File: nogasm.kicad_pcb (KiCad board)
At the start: 2 copper layers, 76.2 x 76.2 mm, 59 parts, among them J1 DC Jack PJ-031DH 3.5mm, J2 DC Jack PRT-10811, Q1 BUK92150-55A, Q2 MMBT2222A, Q3 MMBT2222A, Q4 MMBT2222A, U1 WS2812B, U10 WS2812B, U11 WS2812B, U12 WS2812B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

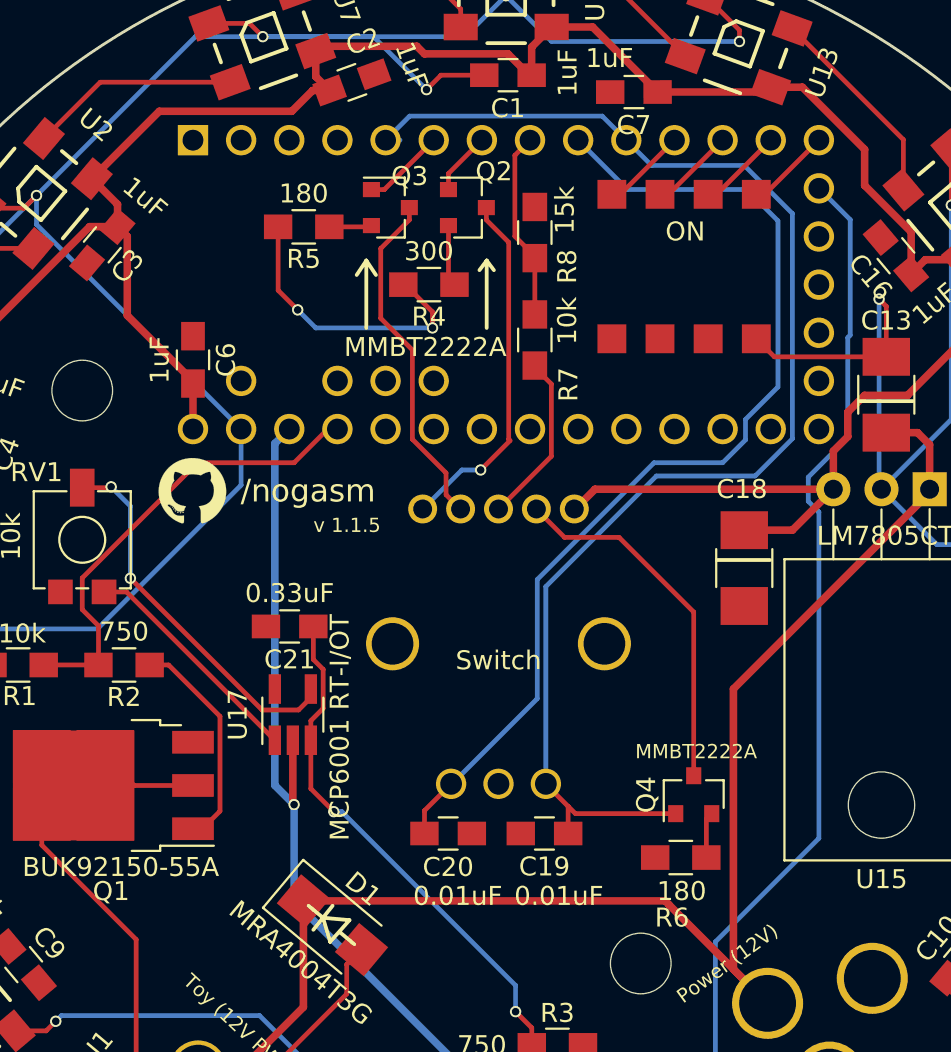
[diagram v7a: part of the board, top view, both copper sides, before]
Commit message: fixing wrong connected ENC_B / ENC_Bl nets
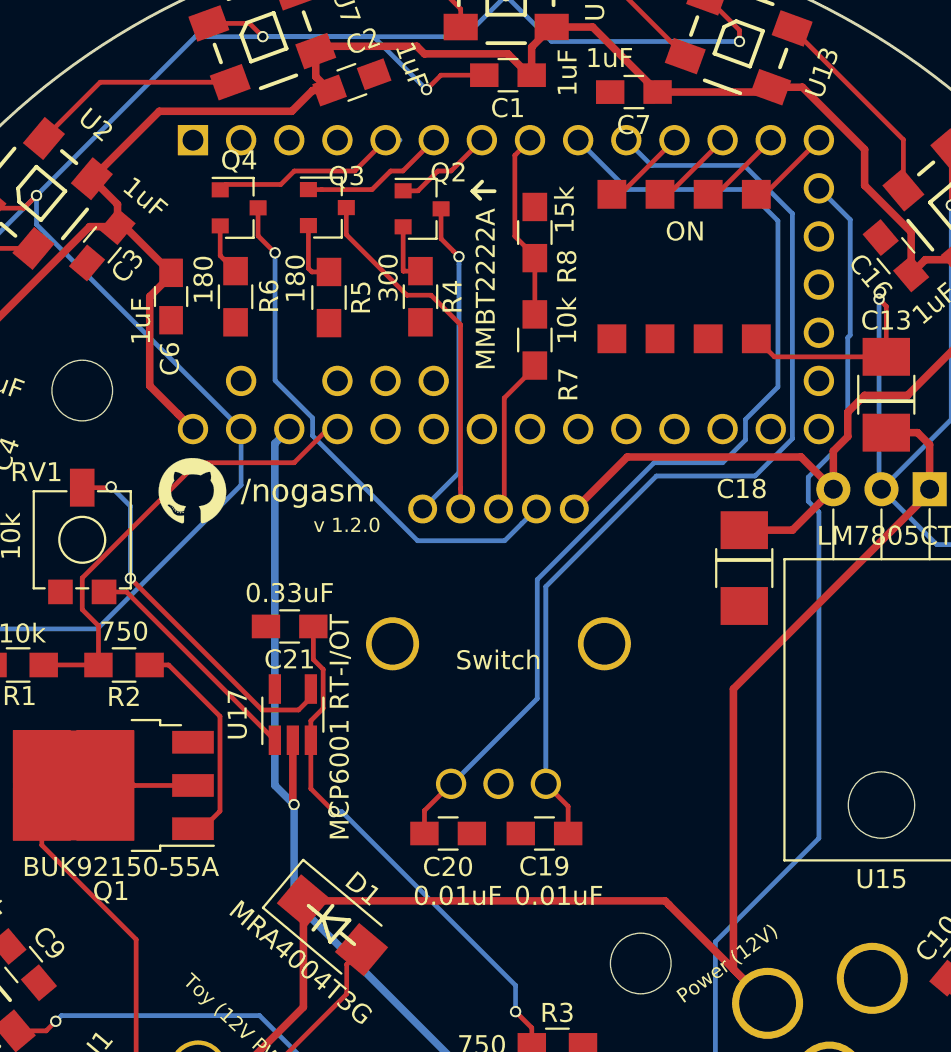
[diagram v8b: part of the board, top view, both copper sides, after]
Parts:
- moved Q4 39.2 mm to (106.3, 62.0), turned to 0 degrees
- moved R6 37.8 mm to (106.1, 66.7), turned to 270 degrees
- moved R5 3.96 mm to (111.1, 66.7), turned to 270 degrees
- moved C6 3.53 mm to (102.7, 66.7), turned to 90 degrees
- moved Q3 3.32 mm to (111.0, 62.0)
- moved Q2 2.39 mm to (116.0, 62.0)
- moved R4 0.78 mm to (115.9, 66.7), turned to 270 degrees
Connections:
- net /ENC_G renamed /ENC_Gr
- net /ENC_R renamed /ENC_Rd
- Q4 pad 1: /ENC_B -> /ENC_Bl
- U5 pad 5: /ENC_B -> /ENC_Bl
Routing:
- net /ENC_B: track 72.3 -> 52.0 mm
- net GND: track 222.4 -> 207.0 mm, vias 13 -> 11
- net /ENC_Bl: track 0.00 -> 10.6 mm
- net Net-(Q4-Pad3): track 19.2 -> 28.0 mm, vias 0 -> 1
- net /ENC_Gr: track 4.37 -> 7.69 mm
- net +5V: track 222.4 -> 224.9 mm
- net /ENC_Rd: track 3.34 -> 5.26 mm
- net Net-(Q2-Pad3): track 18.9 -> 17.0 mm
- net Net-(Q3-Pad2): track 2.25 -> 3.42 mm
- net Net-(Q3-Pad3): track 18.3 -> 19.1 mm
- net Net-(R7-Pad1): track 9.09 -> 8.37 mm
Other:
- board text added: "v 1.2.0"
- board text removed: "v 1.1.5"
